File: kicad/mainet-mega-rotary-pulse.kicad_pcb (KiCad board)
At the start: 2 copper layers, 8 parts, among them J1 Screw_Terminal_01x03, J2 Screw_Terminal_01x03, Q1 BUK9518-55, U1 4N38

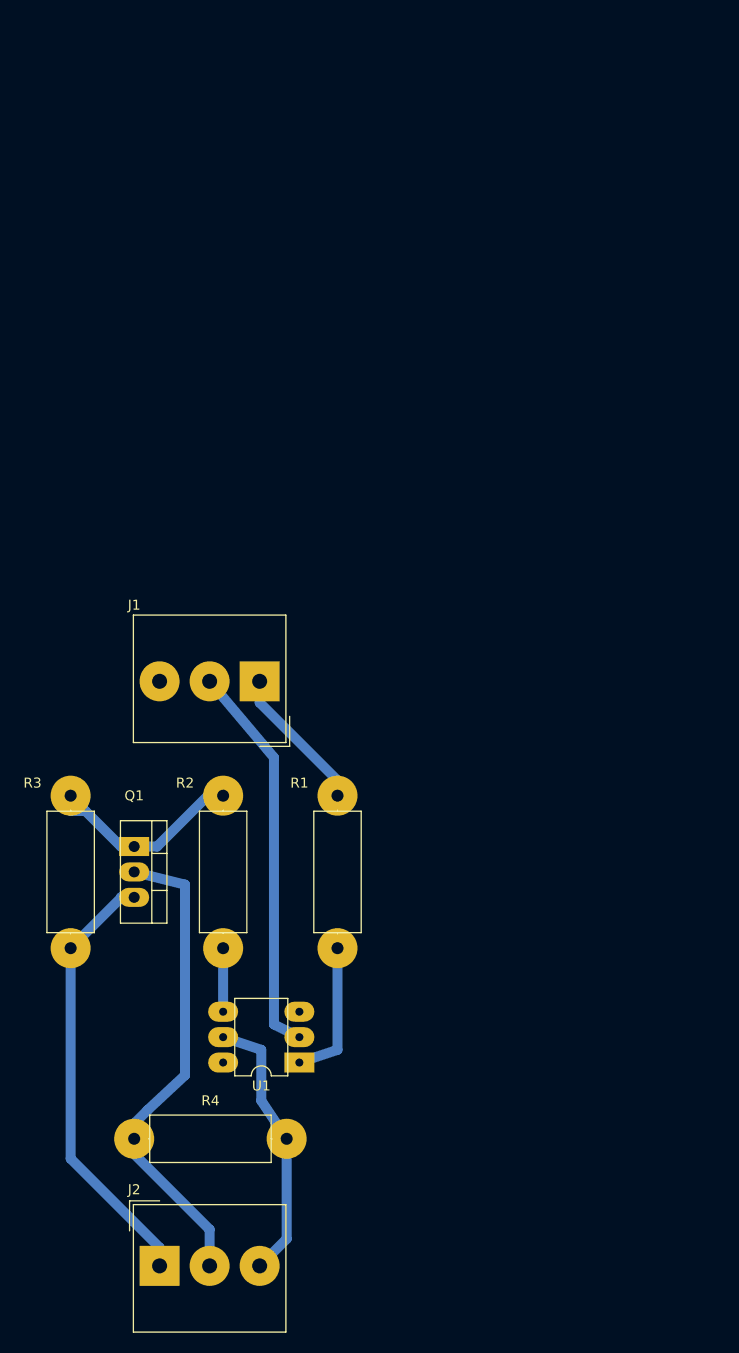
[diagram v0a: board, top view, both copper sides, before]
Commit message: KICAD: Agregar bordes de corte mainet-mega-rotary-pulse.kicad_pcb
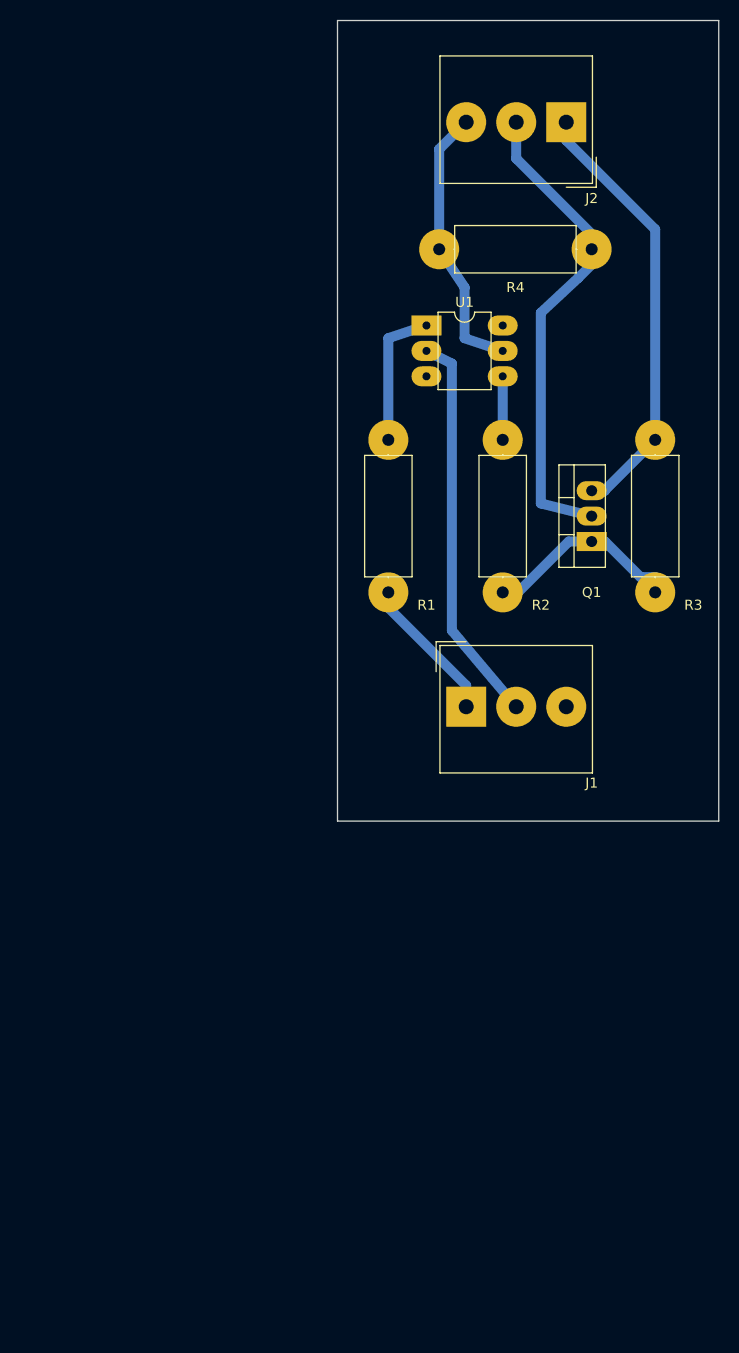
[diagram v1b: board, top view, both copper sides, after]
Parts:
- moved J2 121.3 mm to (188.0, 21.6), turned to 180 degrees
- moved R4 90.2 mm to (175.3, 34.3), turned to 0 degrees
- moved R3 77.4 mm to (196.8, 53.3), turned to 270 degrees
- moved U1 74.7 mm to (174.0, 41.9), turned to 0 degrees
- moved R2 58.0 mm to (181.6, 53.3), turned to 270 degrees
- moved Q1 54.9 mm to (190.5, 63.5), turned to 90 degrees
- moved R1 51.1 mm to (170.2, 53.3), turned to 270 degrees
- moved J1 20.8 mm to (178.0, 80.0), turned to 0 degrees
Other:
- board outline added: 38.1 x 80 mm

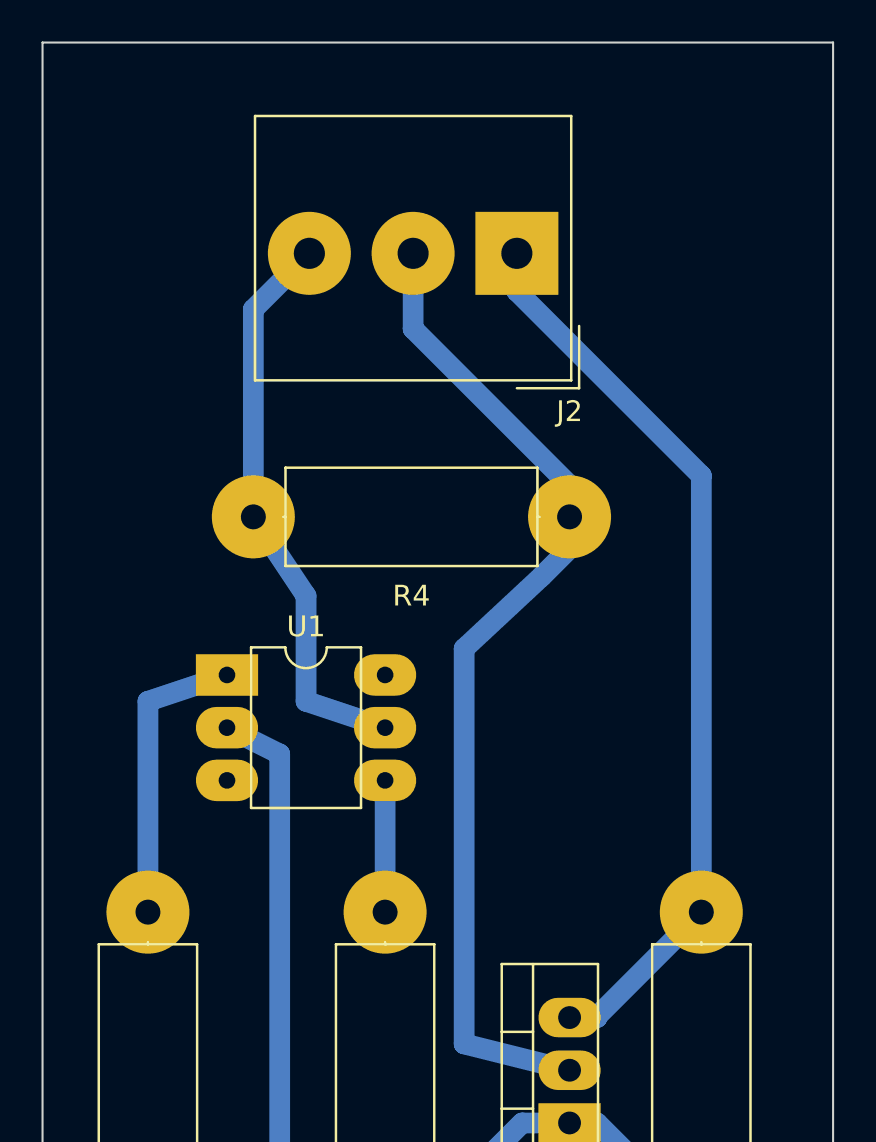
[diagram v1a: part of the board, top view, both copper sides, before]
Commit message: KICAD: Agregar plano de tierra mainet-mega-rotary-pulse.kicad_pcb
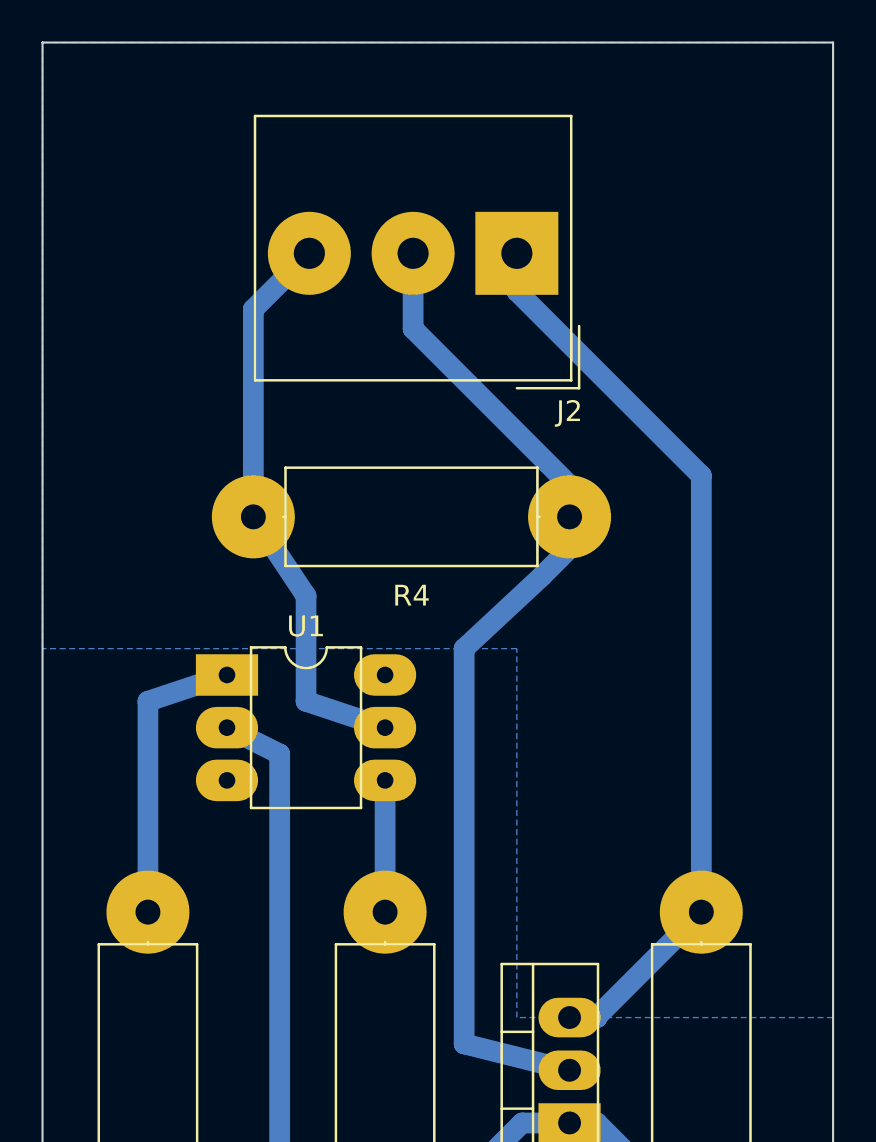
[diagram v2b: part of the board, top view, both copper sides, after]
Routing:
- added copper zone on B.Cu, net GNDD
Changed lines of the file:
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@@
   (segment (start 170.18 53.34) (end 170.18 43.18) (width 1) (layer B.Cu) (net 8))
   (segment (start 181.61 46.99) (end 181.61 53.34) (width 1) (layer B.Cu) (net 9))
+  (zone (net 4) (net_name GNDD) (layer B.Cu) (hatch edge 0.508)
+    (connect_pads (clearance 1))
+    (min_thickness 1)
+    (fill yes (arc_segments 32) (thermal_gap 1.2) (thermal_bridge_width 1.2))
+    (polygon
+      (pts
+        (xy 165.1 11.43) (xy 203.2 11.43) (xy 203.2 58.42) (xy 187.96 58.42) (xy 187.96 40.64)
+        (xy 165.1 40.64)
+      )
+    )
+  )
 )

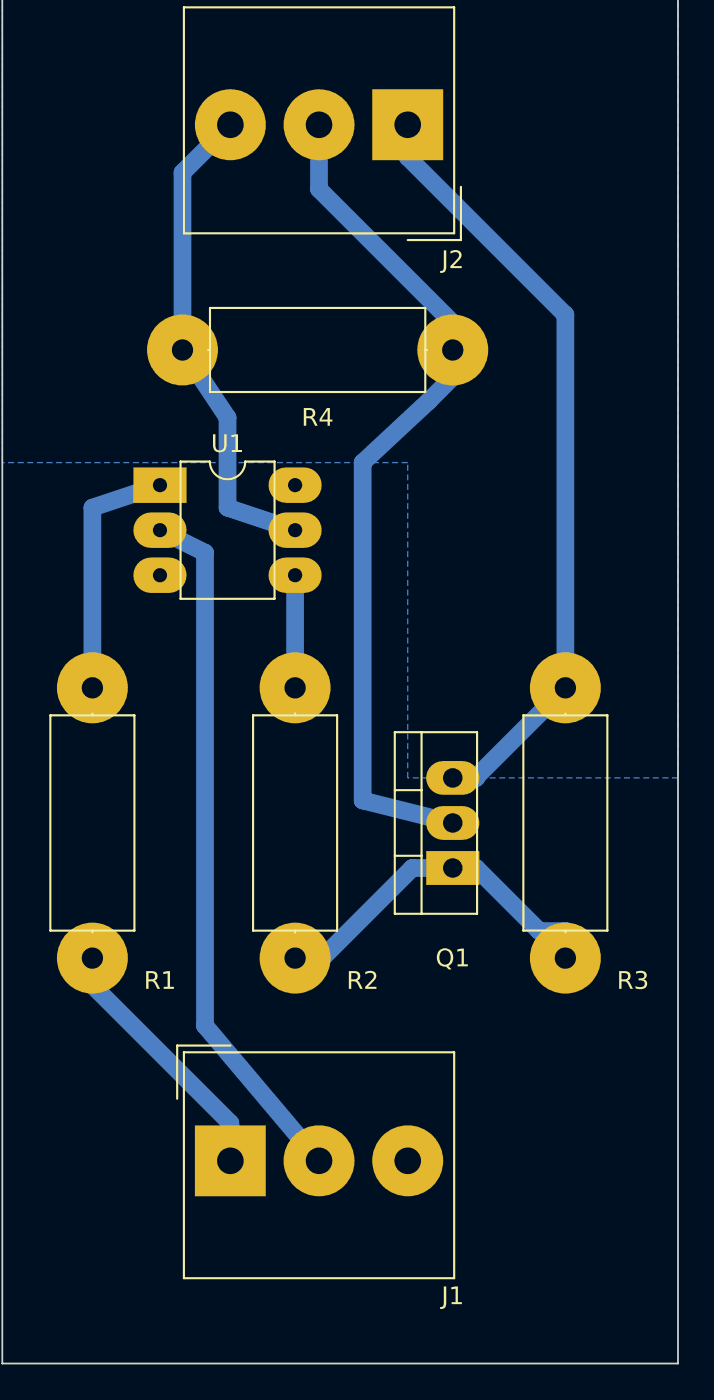
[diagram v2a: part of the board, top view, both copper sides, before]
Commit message: Agregar capa anterior de serigrafía
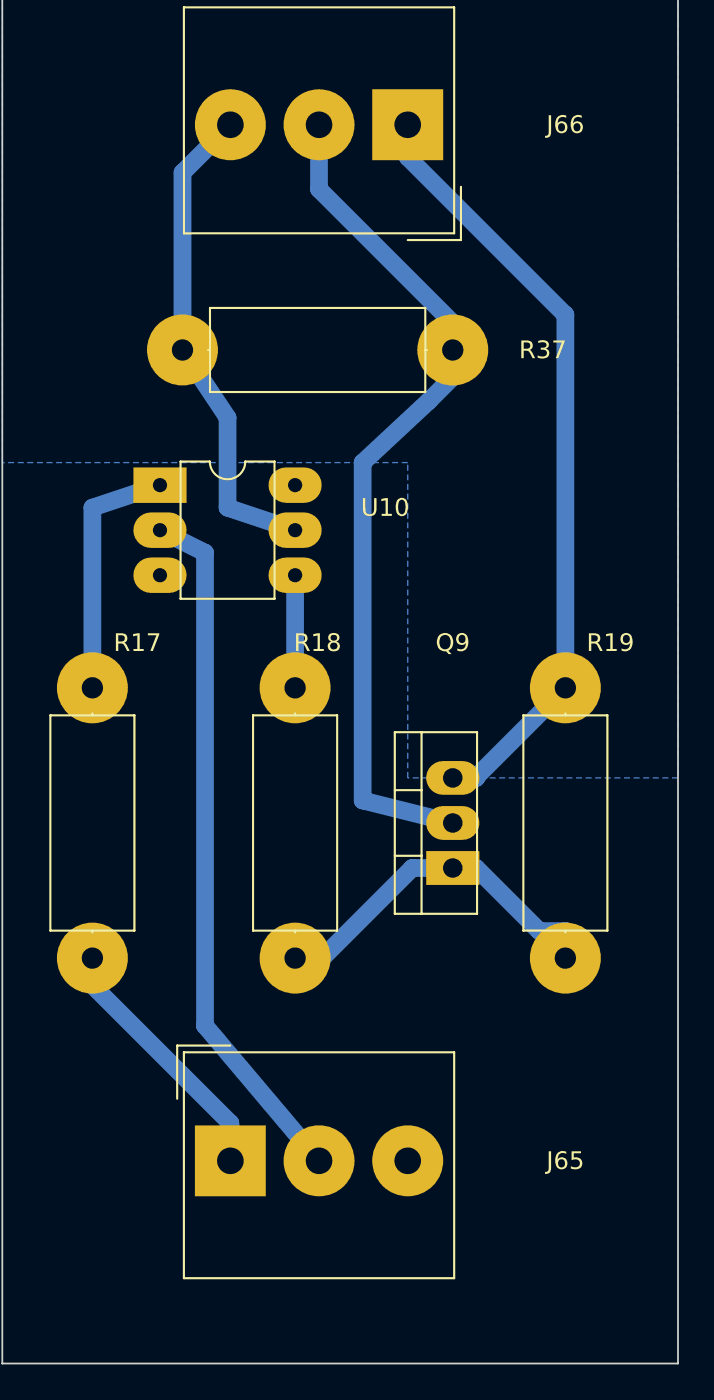
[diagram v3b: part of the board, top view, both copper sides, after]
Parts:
- renumbered J1 to J65, J2 to J66, Q1 to Q9, R1 to R17, R2 to R18, R3 to R19, R4 to R37, U1 to U10
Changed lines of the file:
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@@
     (descr "Resistor, Axial_DIN0414 series, Axial, Horizontal, pin pitch=15.24mm, 2W, length*diameter=11.9*4.5mm^2, http://www.vishay.com/docs/20128/wkxwrx.pdf")
     (tags "Resistor Axial_DIN0414 series Axial Horizontal pin pitch 15.24mm 2W length 11.9mm diameter 4.5mm")
-    (fp_text reference R1 (at 16.51 -3.81 180) (layer F.SilkS)
+    (fp_text reference R17 (at -2.54 -2.54 180) (layer F.SilkS)
       (effects (font (size 1 1) (thickness 0.15)))
     )
@@
     (descr "Resistor, Axial_DIN0414 series, Axial, Horizontal, pin pitch=15.24mm, 2W, length*diameter=11.9*4.5mm^2, http://www.vishay.com/docs/20128/wkxwrx.pdf")
     (tags "Resistor Axial_DIN0414 series Axial Horizontal pin pitch 15.24mm 2W length 11.9mm diameter 4.5mm")
-    (fp_text reference R2 (at 16.51 -3.81 180) (layer F.SilkS)
+    (fp_text reference R18 (at -2.54 -1.27 180) (layer F.SilkS)
       (effects (font (size 1 1) (thickness 0.15)))
     )
@@
     (descr "Resistor, Axial_DIN0414 series, Axial, Horizontal, pin pitch=15.24mm, 2W, length*diameter=11.9*4.5mm^2, http://www.vishay.com/docs/20128/wkxwrx.pdf")
     (tags "Resistor Axial_DIN0414 series Axial Horizontal pin pitch 15.24mm 2W length 11.9mm diameter 4.5mm")
-    (fp_text reference R3 (at 16.51 -3.81) (layer F.SilkS)
+    (fp_text reference R19 (at -2.54 -2.54) (layer F.SilkS)
       (effects (font (size 1 1) (thickness 0.15)))
     )
@@
     (descr "Resistor, Axial_DIN0414 series, Axial, Horizontal, pin pitch=15.24mm, 2W, length*diameter=11.9*4.5mm^2, http://www.vishay.com/docs/20128/wkxwrx.pdf")
     (tags "Resistor Axial_DIN0414 series Axial Horizontal pin pitch 15.24mm 2W length 11.9mm diameter 4.5mm")
-    (fp_text reference R4 (at 7.62 3.81) (layer F.SilkS)
+    (fp_text reference R37 (at 20.32 0) (layer F.SilkS)
       (effects (font (size 1 1) (thickness 0.15)))
     )
@@
     (descr "Altech AK300 serie terminal block (Script generated with StandardBox.py) (http://www.altechcorp.com/PDFS/PCBMETRC.PDF)")
     (tags "Altech AK300 serie connector")
-    (fp_text reference J1 (at 12.54 7.62) (layer F.SilkS)
+    (fp_text reference J65 (at 18.89 0) (layer F.SilkS)
       (effects (font (size 1 1) (thickness 0.15)))
     )
@@
     (descr "Altech AK300 serie terminal block (Script generated with StandardBox.py) (http://www.altechcorp.com/PDFS/PCBMETRC.PDF)")
     (tags "Altech AK300 serie connector")
-    (fp_text reference J2 (at -2.54 -7.62) (layer F.SilkS)
+    (fp_text reference J66 (at -8.89 0) (layer F.SilkS)
       (effects (font (size 1 1) (thickness 0.15)))
     )
@@
     (descr "TO-220-3, Vertical, RM 2.54mm, see https://www.vishay.com/docs/66542/to-220-1.pdf")
     (tags "TO-220-3 Vertical RM 2.54mm")
-    (fp_text reference Q1 (at -5.08 0 180) (layer F.SilkS)
+    (fp_text reference Q9 (at 12.7 0 180) (layer F.SilkS)
       (effects (font (size 1 1) (thickness 0.15)))
     )
@@
     (descr "6-lead though-hole mounted DIP package, row spacing 7.62 mm (300 mils)")
     (tags "THT DIP DIL PDIP 2.54mm 7.62mm 300mil")
-    (fp_text reference U1 (at 3.81 -2.33) (layer F.SilkS)
-      (effects (font (size 1 1) (thickness 0.15)))
-    )
+    (fp_text reference U10 (at 12.7 1.27) (layer F.SilkS)
+      (effects (font (size 1 1) (thickness 0.15)))
+    )
